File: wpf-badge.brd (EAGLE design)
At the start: 74 x 49.3 mm, 6 parts, among them SW1 1825910-6

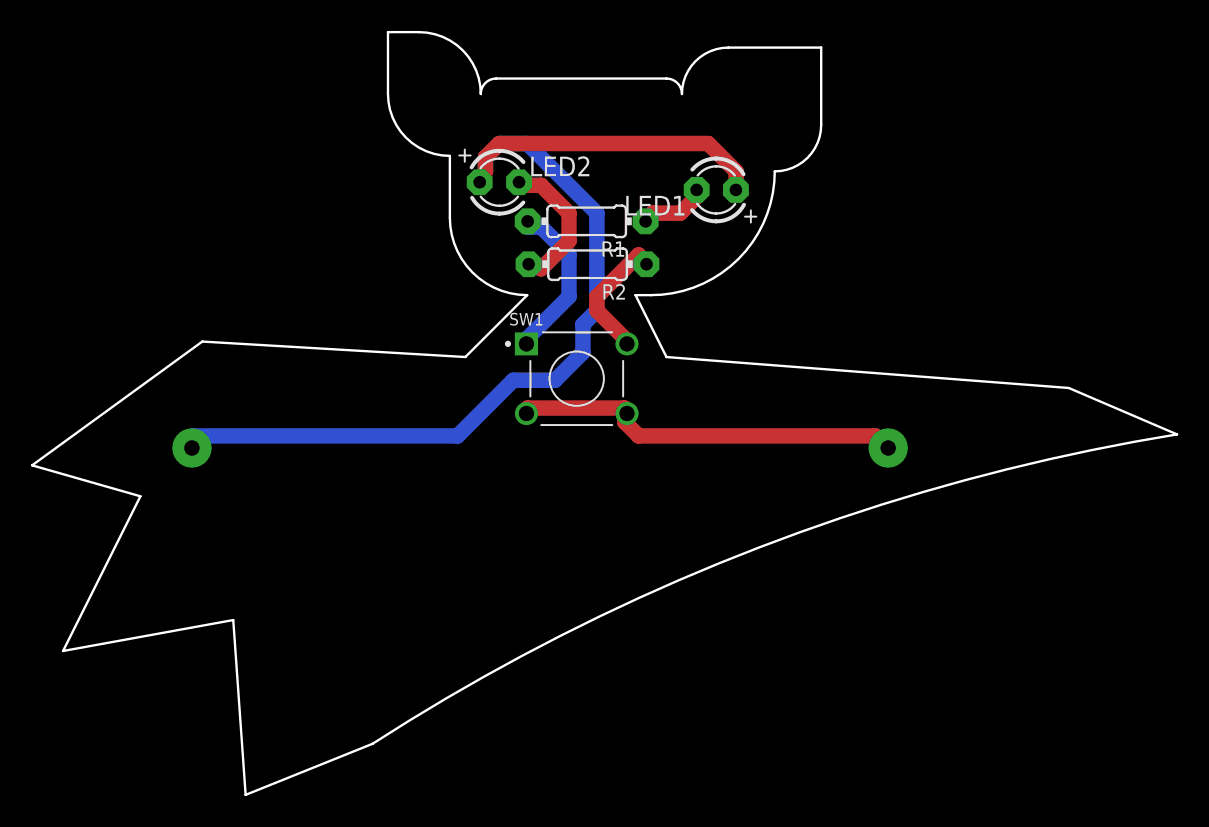
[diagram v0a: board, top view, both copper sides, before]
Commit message: fiddled with the placement of button on board
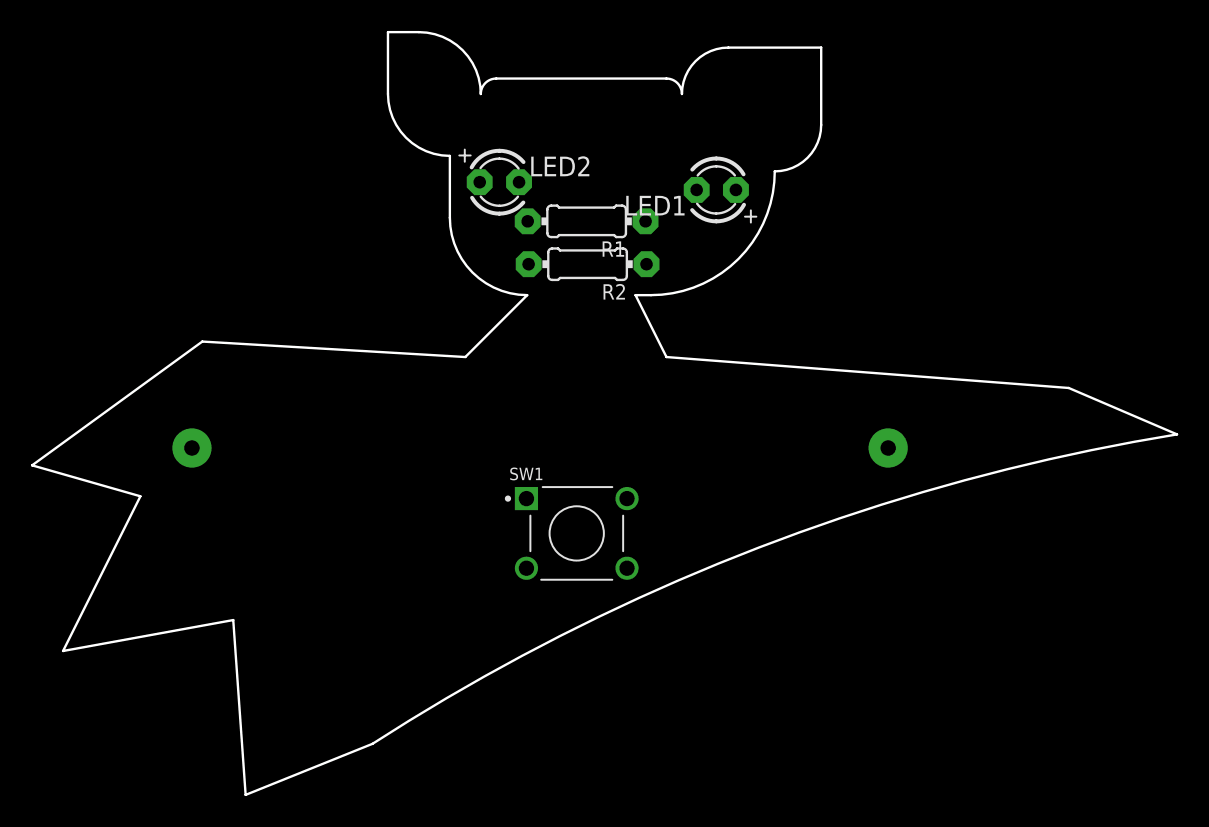
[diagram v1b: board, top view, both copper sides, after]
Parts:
- moved SW1 10.0 mm to (30.2, 12.6)
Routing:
- net N$6: track 68.9 -> 0.00 mm
- net N$3: track 25.3 -> 0.00 mm
- net N$4: track 10.7 -> 0.00 mm
- net N$1: track 9.22 -> 0.00 mm
- net N$5: track 8.43 -> 0.00 mm
- net N$2: track 4.39 -> 0.00 mm
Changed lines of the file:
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@@
 <attribute name="VALUE" x="27.105" y="33.649" size="1.27" layer="27" ratio="10"/>
 </element>
-<element name="SW1" library="1825910-6" package="SW_1825910-6-4" value="1825910-6" x="30.2" y="22.6" smashed="yes">
-<attribute name="COMMENT" value="1825910-6" x="30.2" y="22.6" size="1.778" layer="27" display="off"/>
-<attribute name="CONFIGURATION_POLE-THROW" value="Single Pole - Single Throw" x="30.2" y="22.6" size="1.778" layer="27" display="off"/>
-<attribute name="CONTACT_CURRENT_RATING" value="50 mA" x="30.2" y="22.6" size="1.778" layer="27" display="off"/>
-<attribute name="DESCRIPTION" value=" FSM4JH=6MM TACT SWITCH, HIGH TEMP " x="30.2" y="22.6" size="1.778" layer="27" display="off"/>
-<attribute name="DIGI-KEY_PART_NUMBER" value="450-1650-ND" x="30.2" y="22.6" size="1.778" layer="27" display="off"/>
-<attribute name="DIGI-KEY_PURCHASE_URL" value="https://www.digikey.com/product-detail/en/te-connectivity-alcoswitch-switches/1825910-6/450-1650-ND/1632536?utm_source=snapeda&amp;utm_medium=aggregator&amp;utm_campaign=symbol" x="30.2" y="22.6" size="1.778" layer="27" display="off"/>
-<attribute name="EU_ROHS_COMPLIANCE" value="Compliant" x="30.2" y="22.6" size="1.778" layer="27" display="off"/>
-<attribute name="MF" value="TE Connectivity" x="30.2" y="22.6" size="1.778" layer="27" display="off"/>
-<attribute name="MP" value="1825910-6" x="30.2" y="22.6" size="1.778" layer="27" display="off"/>
-<attribute name="NAME" x="25.835009375" y="26.043940625" size="0.800915625" layer="25"/>
-<attribute name="PACKAGE" value="None" x="30.2" y="22.6" size="1.778" layer="27" display="off"/>
-<attribute name="TE_PURCHASE_URL" value="https://www.te.com/usa-en/product-1825910-6.html?te_bu=Cor&amp;te_type=disp&amp;te_campaign=seda_glo_cor-seda-global-disp-prtnr-fy19-seda-model-bom-cta_sma-317_1&amp;elqCampaignId=32493" x="30.2" y="22.6" size="1.778" layer="27" display="off"/>
-<attribute name="VALUE" x="25.74968125" y="18.239690625" size="0.80005625" layer="27"/>
+<element name="SW1" library="1825910-6" package="SW_1825910-6-4" value="1825910-6" x="30.2" y="12.6" smashed="yes">
+<attribute name="COMMENT" value="1825910-6" x="30.2" y="12.6" size="1.778" layer="27" display="off"/>
+<attribute name="CONFIGURATION_POLE-THROW" value="Single Pole - Single Throw" x="30.2" y="12.6" size="1.778" layer="27" display="off"/>
+<attribute name="CONTACT_CURRENT_RATING" value="50 mA" x="30.2" y="12.6" size="1.778" layer="27" display="off"/>
+<attribute name="DESCRIPTION" value=" FSM4JH=6MM TACT SWITCH, HIGH TEMP " x="30.2" y="12.6" size="1.778" layer="27" display="off"/>
+<attribute name="DIGI-KEY_PART_NUMBER" value="450-1650-ND" x="30.2" y="12.6" size="1.778" layer="27" display="off"/>
+<attribute name="DIGI-KEY_PURCHASE_URL" value="https://www.digikey.com/product-detail/en/te-connectivity-alcoswitch-switches/1825910-6/450-1650-ND/1632536?utm_source=snapeda&amp;utm_medium=aggregator&amp;utm_campaign=symbol" x="30.2" y="12.6" size="1.778" layer="27" display="off"/>
+<attribute name="EU_ROHS_COMPLIANCE" value="Compliant" x="30.2" y="12.6" size="1.778" layer="27" display="off"/>
+<attribute name="MF" value="TE Connectivity" x="30.2" y="12.6" size="1.778" layer="27" display="off"/>
+<attribute name="MP" value="1825910-6" x="30.2" y="12.6" size="1.778" layer="27" display="off"/>
+<attribute name="NAME" x="25.835009375" y="16.043940625" size="0.800915625" layer="25"/>
+<attribute name="PACKAGE" value="None" x="30.2" y="12.6" size="1.778" layer="27" display="off"/>
+<attribute name="TE_PURCHASE_URL" value="https://www.te.com/usa-en/product-1825910-6.html?te_bu=Cor&amp;te_type=disp&amp;te_campaign=seda_glo_cor-seda-global-disp-prtnr-fy19-seda-model-bom-cta_sma-317_1&amp;elqCampaignId=32493" x="30.2" y="12.6" size="1.778" layer="27" display="off"/>
+<attribute name="VALUE" x="25.74968125" y="8.239690625" size="0.80005625" layer="27"/>
 </element>
 </elements>
@@
 <contactref element="LED1" pad="K"/>
 <contactref element="R1" pad="1"/>
-<wire x1="36.9" y1="33.3" x2="35.1" y2="33.3" width="1" layer="1"/>
-<wire x1="37.8" y1="34.2" x2="36.9" y2="33.3" width="1" layer="1"/>
-<wire x1="35.1" y1="33.3" x2="34.65" y2="32.77" width="1" layer="1"/>
-<wire x1="37.8" y1="34.2" x2="37.95" y2="34.8" width="1" layer="1"/>
+<wire x1="34.65" y1="32.77" x2="37.95" y2="34.8" width="0" layer="19" extent="1-1"/>
 </signal>
 <signal name="N$3">
@@
 <contactref element="SW1" pad="3"/>
 <contactref element="SW1" pad="4"/>
-<wire x1="33.3" y1="20.7" x2="27" y2="20.7" width="1" layer="1"/>
-<wire x1="27" y1="20.7" x2="26.95" y2="20.35" width="1" layer="1"/>
-<wire x1="33.3" y1="20.7" x2="33.45" y2="20.35" width="1" layer="1"/>
-<wire x1="34.2" y1="18.9" x2="49.5" y2="18.9" width="1" layer="1"/>
-<wire x1="33.3" y1="19.8" x2="34.2" y2="18.9" width="1" layer="1"/>
-<wire x1="49.5" y1="18.9" x2="50.33" y2="18.12" width="1" layer="1"/>
-<wire x1="33.3" y1="19.8" x2="33.45" y2="20.35" width="1" layer="1"/>
+<wire x1="33.45" y1="10.35" x2="50.33" y2="18.12" width="0" layer="19" extent="1-1"/>
+<wire x1="26.95" y1="10.35" x2="33.45" y2="10.35" width="0" layer="19" extent="1-1"/>
 </signal>
 <signal name="N$1">
 <contactref element="LED2" pad="K"/>
 <contactref element="R2" pad="2"/>
-<wire x1="27.9" y1="35.1" x2="27" y2="35.1" width="1" layer="1"/>
-<wire x1="29.7" y1="33.3" x2="27.9" y2="35.1" width="1" layer="1"/>
-<wire x1="29.7" y1="31.5" x2="29.7" y2="33.3" width="1" layer="1"/>
-<wire x1="27.9" y1="29.7" x2="29.7" y2="31.5" width="1" layer="1"/>
-<wire x1="27" y1="35.1" x2="26.47" y2="35.3" width="1" layer="1"/>
-<wire x1="27.9" y1="29.7" x2="27.09" y2="30" width="1" layer="1"/>
+<wire x1="27.09" y1="30" x2="26.47" y2="35.3" width="0" layer="19" extent="1-1"/>
 </signal>
 <signal name="N$4">
 <contactref element="R1" pad="2"/>
 <contactref element="SW1" pad="1"/>
-<wire x1="29.7" y1="27.9" x2="27" y2="25.2" width="1" layer="16"/>
-<wire x1="29.7" y1="30.6" x2="29.7" y2="27.9" width="1" layer="16"/>
-<wire x1="27.9" y1="32.4" x2="29.7" y2="30.6" width="1" layer="16"/>
-<wire x1="27" y1="32.4" x2="27.9" y2="32.4" width="1" layer="16"/>
-<wire x1="27" y1="25.2" x2="26.95" y2="24.85" width="1" layer="16"/>
-<wire x1="27" y1="32.4" x2="27.03" y2="32.77" width="1" layer="16"/>
+<wire x1="26.95" y1="14.85" x2="27.03" y2="32.77" width="0" layer="19" extent="1-1"/>
 </signal>
 <signal name="N$5">
 <contactref element="R2" pad="1"/>
 <contactref element="SW1" pad="2"/>
-<wire x1="31.5" y1="27" x2="33.3" y2="25.2" width="1" layer="1"/>
-<wire x1="31.5" y1="27.9" x2="31.5" y2="27" width="1" layer="1"/>
-<wire x1="34.2" y1="30.6" x2="31.5" y2="27.9" width="1" layer="1"/>
-<wire x1="33.3" y1="25.2" x2="33.45" y2="24.85" width="1" layer="1"/>
-<wire x1="34.2" y1="30.6" x2="34.71" y2="30" width="1" layer="1"/>
+<wire x1="33.45" y1="14.85" x2="34.71" y2="30" width="0" layer="19" extent="1-1"/>
 </signal>
 <signal name="N$6">
@@
 <contactref element="LED1" pad="A"/>
 <contactref element="LED2" pad="A"/>
-<wire x1="24.3" y1="36.9" x2="24.3" y2="36" width="1" layer="1"/>
-<wire x1="25.2" y1="37.8" x2="24.3" y2="36.9" width="1" layer="1"/>
-<wire x1="38.7" y1="37.8" x2="25.2" y2="37.8" width="1" layer="1"/>
-<wire x1="40.5" y1="36" x2="38.7" y2="37.8" width="1" layer="1"/>
-<wire x1="40.5" y1="35.1" x2="40.5" y2="36" width="1" layer="1"/>
-<wire x1="24.3" y1="36" x2="23.93" y2="35.3" width="1" layer="1"/>
-<wire x1="40.5" y1="35.1" x2="40.49" y2="34.8" width="1" layer="1"/>
-<wire x1="22.5" y1="18.9" x2="5.4" y2="18.9" width="1" layer="16"/>
-<wire x1="26.1" y1="22.5" x2="22.5" y2="18.9" width="1" layer="16"/>
-<wire x1="28.8" y1="22.5" x2="26.1" y2="22.5" width="1" layer="16"/>
-<wire x1="30.6" y1="24.3" x2="28.8" y2="22.5" width="1" layer="16"/>
-<wire x1="30.6" y1="26.1" x2="30.6" y2="24.3" width="1" layer="16"/>
-<wire x1="31.5" y1="27" x2="30.6" y2="26.1" width="1" layer="16"/>
-<wire x1="31.5" y1="33.3" x2="31.5" y2="27" width="1" layer="16"/>
-<wire x1="27" y1="37.8" x2="31.5" y2="33.3" width="1" layer="16"/>
-<wire x1="25.2" y1="37.8" x2="27" y2="37.8" width="1" layer="16"/>
-<wire x1="24.3" y1="36.9" x2="25.2" y2="37.8" width="1" layer="16"/>
-<wire x1="24.3" y1="36" x2="24.3" y2="36.9" width="1" layer="16"/>
-<wire x1="5.4" y1="18.9" x2="5.33" y2="18.12" width="1" layer="16"/>
-<wire x1="24.3" y1="36" x2="23.93" y2="35.3" width="1" layer="16"/>
+<wire x1="23.93" y1="35.3" x2="40.49" y2="34.8" width="0" layer="19" extent="1-1"/>
+<wire x1="5.33" y1="18.12" x2="23.93" y2="35.3" width="0" layer="19" extent="1-1"/>
 </signal>
 </signals>

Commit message: Tweak more board positioning. Minor update to schematic.
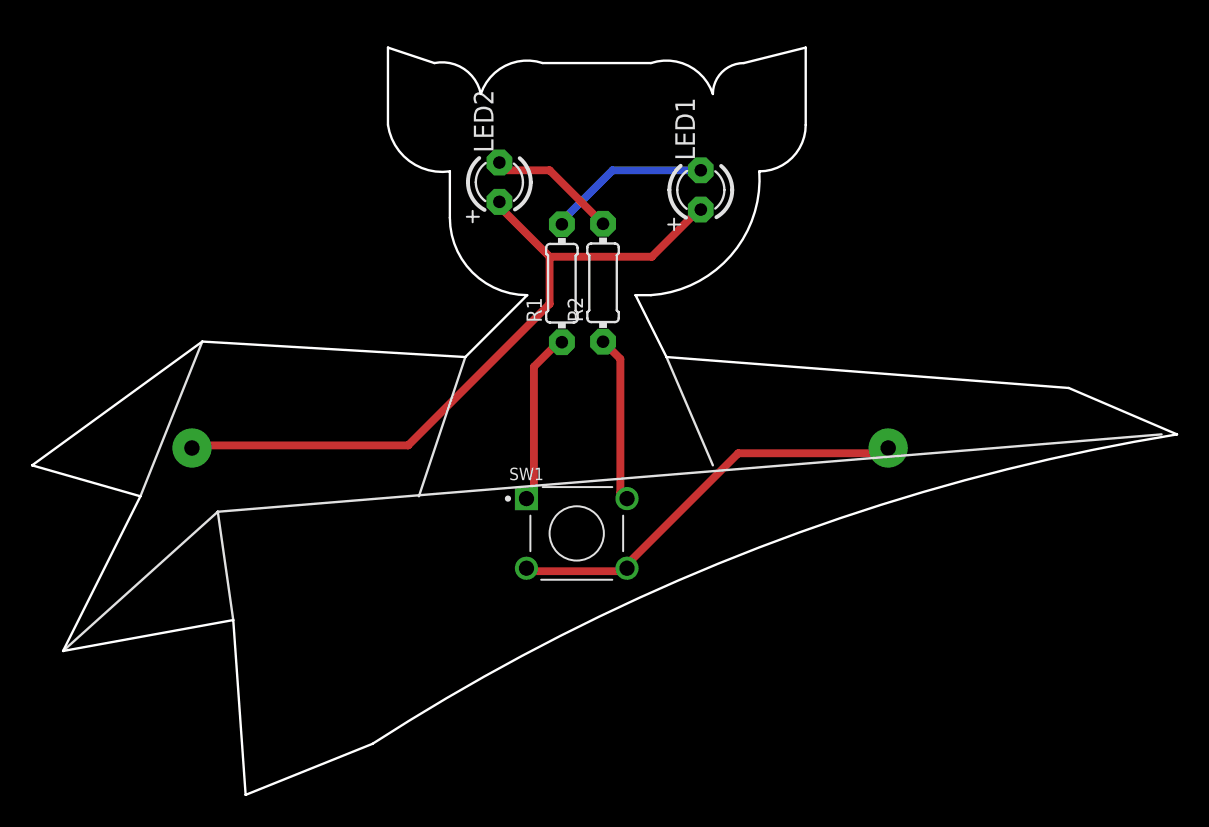
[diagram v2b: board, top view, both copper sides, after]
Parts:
- moved R1 4.31 mm to (29.2, 28.8), turned to 90 degrees
- moved R2 1.56 mm to (31.9, 28.8), turned to 90 degrees
- moved LED1 1.00 mm to (38.2, 34.8), turned to 90 degrees
- turned LED2 to 90 degrees
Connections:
- net N$2: now also R1.2; no longer R1.1
- net N$4: now also R1.1; no longer R1.2
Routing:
- net N$6: track 0.00 -> 45.9 mm
- net N$3: track 0.00 -> 27.0 mm
- net N$4: track 0.00 -> 11.2 mm
- net N$5: track 0.00 -> 10.8 mm
- net N$2: track 0.00 -> 10.5 mm
- net N$1: track 0.00 -> 8.47 mm
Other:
- board size 74 x 49.3 mm -> 74 x 48.3 mm
